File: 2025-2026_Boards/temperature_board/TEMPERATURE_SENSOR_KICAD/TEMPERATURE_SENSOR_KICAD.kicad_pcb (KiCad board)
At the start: 2 copper layers, 103 parts, among them J1 LCD Connector Pinout, J10 Conn_01x03_Pin, J11 Conn_01x03_Pin, J12 Conn_01x02_Pin, J13 Conn_01x02_Pin, J14 Conn_01x02_Pin, J15 Conn_01x02_Pin, J16 Conn_01x02_Pin, J17 Conn_01x02_Pin, J18 Conn_01x02_Pin, J19 Conn_01x02_Pin, J2 Conn_01x02_Pin, J20 Conn_01x02_Pin, J21 Conn_01x02_Pin, J22 Conn_01x02_Pin, J23 Conn_01x02_Pin, J24 Conn_01x02_Pin, J25 Conn_01x02_Pin, J3 Conn_01x02_Pin, J4 Conn_01x03_Pin, J5 Conn_01x03_Pin, J6 Conn_01x03_Pin, J7 Conn_01x03_Pin, J8 Conn_01x03_Pin, J9 Conn_01x03_Pin, U1 STM32G431CBT6, U2 TMP235A4DBZR, U3 AMS1117-3.3, U5 TPS62932DRLR, U6 TPS62932DRLR, U8 AMS1117

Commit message: Worked on PCB. Have to change some track widths.
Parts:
- added J4: Conn_01x02_Pin, Connector_JST:JST_EH_B2B-EH-A_1x02_P2.50mm_Vertical, F.Cu at (33.0, 90.0)
- added J4: Conn_01x02_Pin, Connector_JST:JST_EH_B2B-EH-A_1x02_P2.50mm_Vertical, F.Cu at (113.2, 85.2)
- added J5: Conn_01x02_Pin, Connector_JST:JST_EH_B2B-EH-A_1x02_P2.50mm_Vertical, F.Cu at (119.0, 85.2)
- added J5: Conn_01x02_Pin, Connector_JST:JST_EH_B2B-EH-A_1x02_P2.50mm_Vertical, F.Cu at (33.0, 95.8)
- added J6: Conn_01x02_Pin, Connector_JST:JST_EH_B2B-EH-A_1x02_P2.50mm_Vertical, F.Cu at (33.0, 101.7)
- added J6: Conn_01x02_Pin, Connector_JST:JST_EH_B2B-EH-A_1x02_P2.50mm_Vertical, F.Cu at (124.9, 85.2)
- added J7: Conn_01x02_Pin, Connector_JST:JST_EH_B2B-EH-A_1x02_P2.50mm_Vertical, F.Cu at (33.0, 107.5)
- added J7: Conn_01x02_Pin, Connector_JST:JST_EH_B2B-EH-A_1x02_P2.50mm_Vertical, F.Cu at (130.8, 85.2)
- added J8: Conn_01x02_Pin, Connector_JST:JST_EH_B2B-EH-A_1x02_P2.50mm_Vertical, F.Cu at (33.0, 113.3)
- moved Cboot2 607.3 mm to (58.5, 135.7)
- moved Cinx2 607.3 mm to (53.5, 136.5)
- moved L2 607.3 mm to (64.0, 143.5)
- moved Rfbt2 607.3 mm to (59.7, 134.0)
- moved U5 607.3 mm to (56.1, 135.2)
- moved Rfbb2 607.3 mm to (59.5, 132.5)
- moved Cout2 590.4 mm to (64.5, 134.5)
- moved Css2 590.1 mm to (56.8, 133.0)
- moved C1 518.3 mm to (175.0, 128.4)
- moved C2 518.3 mm to (175.0, 125.0)
- moved C3 518.3 mm to (175.5, 122.2)
- moved D1 518.3 mm to (174.0, 122.8)
- moved R1 518.3 mm to (173.3, 124.3), turned to -90 degrees
- moved U3 518.3 mm to (180.5, 124.0)
- moved J4 511.9 mm to (31.0, 50.0)
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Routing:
- net GND: track 6.56 -> 26.4 mm, vias 0 -> 18
- net +2.2V: track 2.56 -> 8.12 mm
- net Net-(U6-FB): track 0.00 -> 3.63 mm
- net Net-(U5-SS): track 0.00 -> 2.75 mm
- net 5V: track 13.0 -> 15.8 mm
- net 12V: track 13.4 -> 15.5 mm
- net Net-(U5-FB): track 2.06 -> 3.61 mm
- net +3.3V: track 11.2 -> 12.5 mm
- net /PWR_LED_K: track 0.00 -> 1.14 mm
- net Net-(D35-K): track 0.00 -> 1.04 mm

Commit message: Fan connectors broken+buggy. Fixed it. Accidentally deleted ground plane. Will have to add back. To get done by start of work session on Sunday: Hook up all fan connectors. Hook up temperature sensor to microcontroller. Hook up power distributor to microcontroller. At work session: Figure out LCD-diode wiring
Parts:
- removed J22, J23, J24, J25: Conn_01x02_Pin, Connector_JST:JST_EH_B2B-EH-A_1x02_P2.50mm_Vertical
- removed the J4 at (33.0, 90.0)
- removed the J4 at (113.2, 85.2)
- removed the J4 at (31.0, 50.0)
- removed the J5 at (31.0, 58.0)
- removed the J5 at (119.0, 85.2)
- removed the J5 at (33.0, 95.8)
- removed the J6 at (33.0, 101.7)
- removed the J6 at (31.0, 65.8)
- removed the J6 at (124.9, 85.2)
- removed the J7 at (33.0, 107.5)
- removed the J7 at (31.0, 73.8)
- removed the J7 at (130.8, 85.2)
- removed the J8 at (33.0, 113.3)
- removed the J8 at (31.0, 81.7)
- added J4: Conn_01x02_Pin, Connector:FanPinHeader_1x03_P2.54mm_Vertical, F.Cu at (21.5, 128.0)
- added J5: Conn_01x02_Pin, Connector:FanPinHeader_1x03_P2.54mm_Vertical, F.Cu at (21.5, 119.5)
- added J6: Conn_01x02_Pin, Connector:FanPinHeader_1x03_P2.54mm_Vertical, F.Cu at (21.5, 169.5)
- added J7: Conn_01x02_Pin, Connector:FanPinHeader_1x03_P2.54mm_Vertical, F.Cu at (21.5, 178.0)
- added J8: Conn_01x02_Pin, Connector:FanPinHeader_1x03_P2.54mm_Vertical, F.Cu at (21.5, 186.0)
- J10, J11, J9: value Conn_01x03_Pin -> Conn_01x02_Pin
- J12, J13, J14, J15, J16, J17, J18, J19, J2, J20, J21, J3: footprint Connector_JST:JST_EH_B2B-EH-A_1x02_P2.50mm_Vertical -> Connector:FanPinHeader_1x03_P2.54mm_Vertical
- moved J2 539.3 mm to (16.4, 193.5)
- moved J12 522.9 mm to (21.5, 161.0), turned to 180 degrees
- moved J14 517.8 mm to (21.5, 144.5), turned to 180 degrees
- moved J17 516.1 mm to (17.0, 88.5)
- moved J13 513.4 mm to (21.5, 103.0), turned to 180 degrees
- moved J16 455.4 mm to (79.8, 120.1)
- moved J15 439.4 mm to (95.4, 109.6)
- moved J3 438.7 mm to (94.9, 70.6)
- moved U2 276.1 mm to (164.9, 134.0)
- moved Cout1 152.9 mm to (74.7, 57.1), turned to 90 degrees
- moved Rfbb1 149.6 mm to (77.7, 58.6), turned to 0 degrees
- moved L3 148.4 mm to (86.0, 56.5), turned to 90 degrees
- moved Rfbt1 147.9 mm to (77.1, 60.1), turned to 0 degrees
- moved Css1 147.5 mm to (78.7, 59.9), turned to 90 degrees
- moved Cboot1 146.6 mm to (80.2, 60.1), turned to 0 degrees
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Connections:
- J10 pad 1: +12V -> 5V
- J10 pad 3: ECORE FAN PINS -> (no net)
- J11 pad 1: +12V -> 5V
- J11 pad 3: ECORE FAN PINS -> (no net)
- J12 pad 1: +12V -> 5V
- J13 pad 1: +12V -> 5V
- J14 pad 1: +12V -> 5V
- J15 pad 1: +12V -> 12V
- J16 pad 1: +12V -> 12V
- J17 pad 1: +12V -> 12V
- J18 pad 1: +5V -> 12V
- J19 pad 1: +5V -> 12V
- J2 pad 1: +12V -> 5V
- J20 pad 1: +5V -> 12V
- J21 pad 1: +5V -> 12V
- J3 pad 1: +12V -> 12V
- J9 pad 1: +12V -> 5V
- J9 pad 3: ECORE FAN PINS -> (no net)
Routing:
- net 5V: track 15.8 -> 99.5 mm
- net GND: track 26.4 -> 71.4 mm, vias 18 -> 30
- removed copper zone on B.Cu, net GND

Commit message: Kept wiring. To-do tomorrow: add back ground plane. Hook up ground vias. Wire LCD. Potentially reorganize the fan connectors. Wire fans together.
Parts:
- moved C13 453.5 mm to (42.5, 108.0)
- moved C8 449.7 mm to (49.0, 109.5), turned to 180 degrees
- moved C4 449.5 mm to (51.0, 108.5), turned to -90 degrees
- moved C9 448.6 mm to (49.0, 110.5), turned to 180 degrees
- moved C12 442.6 mm to (42.5, 107.0)
- moved C14 432.0 mm to (42.5, 103.0)
- moved R2 426.0 mm to (42.5, 104.0), turned to 180 degrees
- moved C11 422.1 mm to (42.3, 106.0)
- moved C10 411.2 mm to (49.0, 111.5)
- moved C5 405.1 mm to (52.0, 108.5), turned to -90 degrees
- moved FB1 402.6 mm to (47.0, 110.5), turned to -90 degrees
- moved C7 396.9 mm to (54.0, 108.5), turned to -90 degrees
- moved C6 393.3 mm to (53.0, 108.5), turned to -90 degrees
- moved C24 160.5 mm to (52.0, 156.4)
- moved C25 160.5 mm to (52.0, 154.0)
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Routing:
- net +3.3V: track 12.5 -> 48.2 mm
- net +3.3VA: track 0.00 -> 7.82 mm
- net Net-(U1-PA3): track 0.00 -> 2.94 mm
- net Net-(U2-VOUT): track 0.00 -> 1.98 mm
- net Net-(C10-Pad1): track 0.00 -> 1.63 mm
- net Net-(C8-Pad2): track 0.00 -> 1.00 mm

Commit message: Almost finished wiring. Just need to adjust widths and check configuration before finalizing design
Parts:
- removed D10, D11, D12, D13, D14, D15, D16, D17, D18, D19, D20, D21, D22, D23, D24, D25, D26, D27, D28, D29, D3, D30, D31, D32, D33, D34, D4, D5, D6, D7, D8, D9: 1N4148WT, Diode_SMD:D_SOD-523
- moved J1 393.8 mm to (59.9, 102.0), turned to 90 degrees
- moved J17 71.7 mm to (16.2, 20.5), turned to 90 degrees
- moved Cin1 64.3 mm to (22.8, 36.2), turned to -90 degrees
- moved Cin2 63.8 mm to (27.2, 31.2), turned to 0 degrees
- moved J19 62.8 mm to (84.8, 21.0), turned to 90 degrees
- moved J21 62.1 mm to (25.8, 20.5), turned to 90 degrees
- moved Cinx1 61.9 mm to (25.2, 35.8), turned to -90 degrees
- moved U6 60.0 mm to (27.9, 34.5), turned to 0 degrees
- moved Rfbt1 59.9 mm to (30.2, 32.1), turned to -90 degrees
- moved Cout1 59.5 mm to (33.2, 29.7), turned to 0 degrees
- moved Css1 58.0 mm to (30.5, 33.8), turned to 0 degrees
- moved Rfbb1 57.8 mm to (31.8, 32.8), turned to -90 degrees
- moved Cboot1 56.8 mm to (30.2, 35.2), turned to -90 degrees
- moved J20 54.8 mm to (74.8, 20.5), turned to 90 degrees
- moved J3 54.3 mm to (35.2, 20.5), turned to 90 degrees
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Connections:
- C1 pad 1: +5V -> 5V
- C24 pad 1: +5V -> 5V
- J1 pad 1: Net-(D15-K) -> Net-(J1-Pin_1)
- J1 pad 10: Net-(D16-K) -> Net-(J1-Pin_10)
- J1 pad 11: Net-(D11-K) -> Net-(J1-Pin_11)
- J1 pad 12: Net-(D10-A) -> Net-(J1-Pin_12)
- J1 pad 2: Net-(D14-K) -> Net-(J1-Pin_2)
- J1 pad 3: Net-(D10-K) -> Net-(J1-Pin_3)
- J1 pad 4: Net-(D13-K) -> Net-(J1-Pin_4)
- J1 pad 5: Net-(D17-K) -> Net-(J1-Pin_5)
- J1 pad 6: Net-(D27-A) -> Net-(J1-Pin_6)
- J1 pad 7: Net-(D12-K) -> Net-(J1-Pin_7)
- J1 pad 8: Net-(D19-A) -> Net-(J1-Pin_8)
- J1 pad 9: Net-(D11-A) -> Net-(J1-Pin_9)
- U1 pad 17: Net-(D12-K) -> unconnected-(U1-PB1-Pad17)
- U1 pad 25: unconnected-(U1-PB11-Pad25) -> Net-(J1-Pin_1)
- U1 pad 26: unconnected-(U1-PB12-Pad26) -> Net-(J1-Pin_2)
- U1 pad 27: unconnected-(U1-PB13-Pad27) -> Net-(J1-Pin_3)
- U1 pad 28: Net-(D27-A) -> Net-(J1-Pin_4)
- U1 pad 29: Net-(D19-A) -> Net-(J1-Pin_5)
- U1 pad 3: Net-(D11-K) -> unconnected-(U1-PC14-Pad3)
- U1 pad 30: unconnected-(U1-PA8-Pad30) -> Net-(J1-Pin_6)
- U1 pad 31: unconnected-(U1-PA9-Pad31) -> Net-(J1-Pin_7)
- U1 pad 32: unconnected-(U1-PA10-Pad32) -> Net-(J1-Pin_8)
- U1 pad 33: unconnected-(U1-PA11-Pad33) -> Net-(J1-Pin_9)
- U1 pad 34: unconnected-(U1-PA12-Pad34) -> Net-(J1-Pin_10)
- U1 pad 37: unconnected-(U1-PA13-Pad37) -> Net-(J1-Pin_11)
- U1 pad 38: unconnected-(U1-PA14-Pad38) -> Net-(J1-Pin_12)
- U1 pad 4: Net-(D16-K) -> unconnected-(U1-PC15-Pad4)
- U1 pad 40: Net-(D17-K) -> unconnected-(U1-PB3-Pad40)
- U1 pad 41: Net-(D13-K) -> unconnected-(U1-PB4-Pad41)
- U1 pad 42: Net-(D10-K) -> unconnected-(U1-PB5-Pad42)
- U1 pad 43: Net-(D14-K) -> unconnected-(U1-PB6-Pad43)
- U1 pad 44: Net-(D15-K) -> unconnected-(U1-PB7-Pad44)
- U1 pad 5: Net-(D11-A) -> unconnected-(U1-PF0-Pad5)
- U1 pad 7: Net-(D10-A) -> unconnected-(U1-PG10-Pad7)
- U3 pad 3: +5V -> 5V
- U8 pad 3: +5V -> 5V
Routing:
- net 5V: track 99.5 -> 193.6 mm
- net +3.3V: track 48.2 -> 57.6 mm
- net Net-(J1-Pin_12): track 0.00 -> 7.60 mm
- net GND: track 71.4 -> 78.1 mm, vias 30 -> 40
- net Net-(J1-Pin_11): track 0.00 -> 5.99 mm
- net +5V: track 5.47 -> 0.00 mm
- net Net-(J1-Pin_9): track 0.00 -> 3.79 mm
- net Net-(J1-Pin_8): track 0.00 -> 3.79 mm
- net Net-(J1-Pin_7): track 0.00 -> 3.79 mm
- net Net-(J1-Pin_6): track 0.00 -> 3.79 mm
- net Net-(J1-Pin_5): track 0.00 -> 3.79 mm
- net Net-(J1-Pin_4): track 0.00 -> 3.79 mm
- net Net-(J1-Pin_3): track 0.00 -> 3.79 mm
- net Net-(J1-Pin_2): track 0.00 -> 3.79 mm
- net Net-(J1-Pin_10): track 0.00 -> 3.79 mm
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
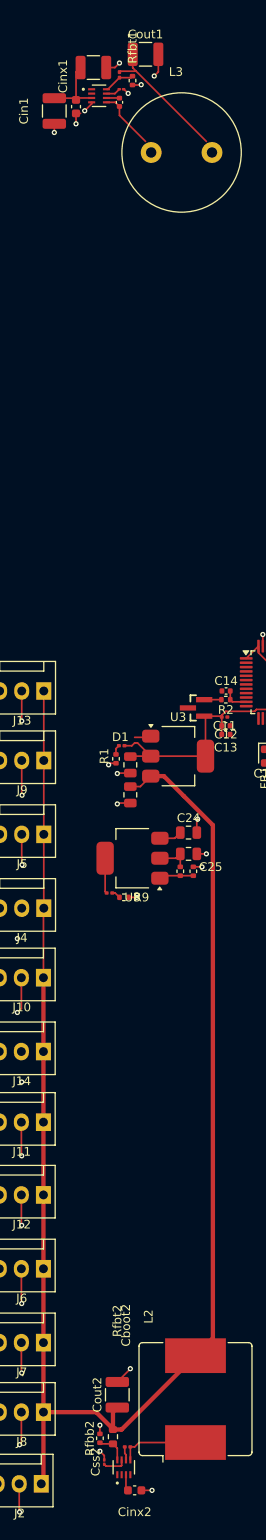
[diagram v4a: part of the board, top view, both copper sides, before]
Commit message: Adjusted widths for voltage safety.
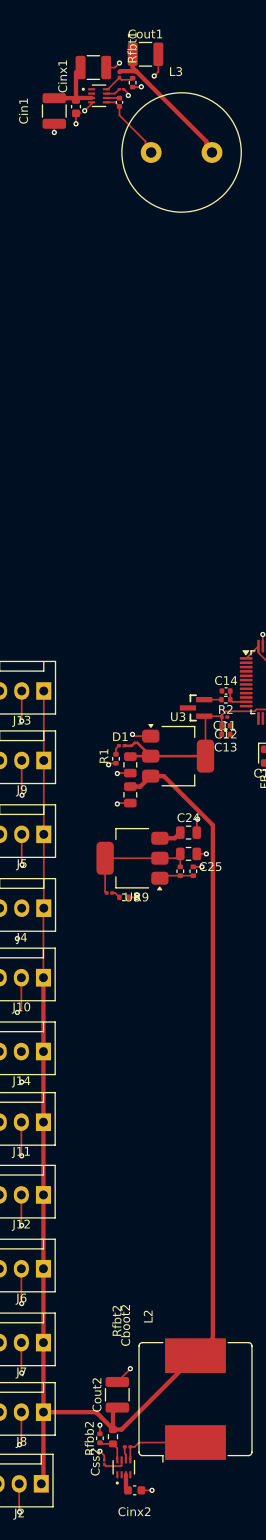
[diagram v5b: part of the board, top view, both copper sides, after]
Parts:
- moved Rfbb1 0.24 mm to (31.8, 33.0)
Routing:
- net +2.2V: track 8.12 -> 14.4 mm
- net Net-(U6-SW): track 6.96 -> 8.51 mm
- net 12V: track 15.5 -> 17.0 mm
- net GND: track 78.1 -> 78.6 mm, vias 40 -> 41
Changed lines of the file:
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@@
 		)
 		(property "Value" "47u"
-			(at 0 2.3 0)
+			(at 0.0175 2.54 0)
 			(layer "F.Fab")
 			(effects
@@
 	(footprint "Resistor_SMD:R_0402_1005Metric"
 		(layer "F.Cu")
-		(at 31.75 32.75 -90)
+		(at 31.7675 32.99 -90)
 		(descr "Resistor SMD 0402 (1005 Metric), square (rectangular) end terminal, IPC-7351 nominal, (Body size source: IPC-SM-782 page 72, https://www.pcb-3d.com/wordpress/wp-content/uploads/ipc-sm-782a_amendment_1_and_2.pdf), generated with kicad-footprint-generator")
 		(tags "resistor")
@@
 	)
 	(segment
+		(start 31.95 108.2)
+		(end 31.75 108)
+		(width 0.2)
+		(layer "F.Cu")
+		(net 1)
+	)
+	(segment
 		(start 31.5 112.45)
 		(end 30.05 112.45)
@@
 	)
 	(segment
-		(start 32 108.335)
-		(end 33.715 108.335)
-		(width 0.2)
-		(layer "F.Cu")
-		(net 1)
-	)
-	(segment
 		(start 27.0482 35.4268)
 		(end 26.25 36.225)
@@
 	)
 	(segment
+		(start 33.85 108.2)
+		(end 31.95 108.2)
+		(width 0.2)
+		(layer "F.Cu")
+		(net 1)
+	)
+	(segment
 		(start 51 108.98)
 		(end 51 110)
@@
 	)
 	(segment
-		(start 31.75 33.26)
-		(end 32.715 33.26)
+		(start 31.7675 33.5)
+		(end 32.7325 33.5)
 		(width 0.2)
 		(layer "F.Cu")
@@
 	)
 	(via
-		(at 32.75 33.225)
+		(at 32.7675 33.465)
+		(size 0.6)
+		(drill 0.3)
+		(layers "F.Cu" "B.Cu")
+		(net 1)
+	)
+	(via
+		(at 31.75 108)
 		(size 0.6)
 		(drill 0.3)
@@
 	)
 	(via
-		(at 31.25 34.225)
+		(at 31.2675 34.465)
 		(size 0.6)
 		(drill 0.3)
@@
 		(start 32.325 108.975)
 		(end 33.85 110.5)
-		(width 0.2)
+		(width 0.3)
 		(layer "F.Cu")
 		(net 2)
@@
 		(start 33.85 110.5)
 		(end 40.15 110.5)
-		(width 0.2)
+		(width 0.3)
 		(layer "F.Cu")
 		(net 2)
@@
 		(start 31.675 109.3)
 		(end 32 108.975)
-		(width 0.2)
+		(width 0.3)
 		(layer "F.Cu")
 		(net 2)
@@
 		(start 32 108.975)
 		(end 32.325 108.975)
-		(width 0.2)
+		(width 0.3)
 		(layer "F.Cu")
 		(net 2)
@@
 		(start 33.85 110.5)
 		(end 31.55 110.5)
-		(width 0.2)
+		(width 0.3)
 		(layer "F.Cu")
 		(net 2)
@@
 		(start 30.825 109.3)
 		(end 31.675 109.3)
-		(width 0.2)
+		(width 0.3)
 		(layer "F.Cu")
 		(net 2)
@@
 	)
 	(segment
+		(start 28.6 122.25)
+		(end 34.9 122.25)
+		(width 0.2)
+		(layer "F.Cu")
+		(net 7)
+	)
+	(segment
 		(start 36.75 122.25)
 		(end 34.9 122.25)
@@
 	)
 	(segment
+		(start 33.25 40.375711)
+		(end 33.8991 41.024811)
+		(width 0.2)
+		(layer "F.Cu")
+		(net 8)
+	)
+	(segment
+		(start 33.25 39.75)
+		(end 33.25 40.375711)
+		(width 0.2)
+		(layer "F.Cu")
+		(net 8)
+	)
+	(segment
 		(start 30.25 35.73)
 		(end 30.25 36.75)
@@
 		(start 22.75 34.775)
 		(end 25.05 34.775)
-		(width 0.2)
+		(width 0.5)
 		(layer "F.Cu")
 		(net 12)
@@
 		(start 25.25 34.975)
 		(end 25.25 31.775)
-		(width 0.2)
+		(width 0.5)
 		(layer "F.Cu")
 		(net 12)
@@
 		(start 25.475126 34.749874)
 		(end 27.0482 34.749874)
-		(width 0.2)
+		(width 0.5)
 		(layer "F.Cu")
 		(net 12)
@@
 		(start 30.999874 193.2018)
 		(end 30.999874 194.774874)
-		(width 0.2)
+		(width 0.5)
 		(layer "F.Cu")
 		(net 12)
@@
 		(start 32.169 31.669)
 		(end 30.356 31.669)
-		(width 0.2)
+		(width 0.5)
+		(layer "F.Cu")
+		(net 13)
+	)
+	(segment
+		(start 40.25 40.375711)
+		(end 40.8991 41.024811)
+		(width 0.5)
 		(layer "F.Cu")
 		(net 13)
@@
 		(start 40.25 39.75)
 		(end 32.169 31.669)
-		(width 0.2)
+		(width 0.5)
+		(layer "F.Cu")
+		(net 13)
+	)
+	(segment
+		(start 40.25 39.75)
+		(end 40.25 40.375711)
+		(width 0.5)
 		(layer "F.Cu")
 		(net 13)
@@
 		(start 30.356 31.669)
 		(end 30.25 31.775)
-		(width 0.2)
+		(width 0.5)
 		(layer "F.Cu")
 		(net 13)
@@
 		(start 31.775 31.275)
 		(end 32.169 31.669)
-		(width 0.2)
+		(width 0.5)
 		(layer "F.Cu")
 		(net 13)
@@
 		(start 31.775 29.725)
 		(end 31.775 31.275)
-		(width 0.2)
+		(width 0.5)
 		(layer "F.Cu")
 		(net 13)
@@
 		(start 31.5 114)
 		(end 32.65 114)
-		(width 0.2)
+		(width 0.5)
 		(layer "F.Cu")
 		(net 14)
@@
 		(start 36.6 119.95)
 		(end 34.9 119.95)
-		(width 0.2)
+		(width 0.5)
 		(layer "F.Cu")
 		(net 14)
@@
 		(start 32.65 114)
 		(end 33.85 112.8)
-		(width 0.2)
+		(width 0.5)
 		(layer "F.Cu")
 		(net 14)
@@
 		(start 37.25 119.3)
 		(end 36.6 119.95)
-		(width 0.2)
+		(width 0.5)
 		(layer "F.Cu")
 		(net 14)
@@
 	)
 	(segment
+		(start 30.5 32.655)
+		(end 30.49 32.655)
+		(width 0.2)
+		(layer "F.Cu")
+		(net 20)
+	)
+	(segment
 		(start 28.915378 33.749622)
 		(end 30.25 32.415)
@@
 	)
 	(segment
-		(start 31.575 32.415)
-		(end 31.75 32.24)
+		(start 31.5925 32.655)
+		(end 31.7675 32.48)
 		(width 0.2)
 		(layer "F.Cu")
@@
 	)
 	(segment
-		(start 30.25 32.415)
-		(end 31.575 32.415)
+		(start 30.5 32.655)
+		(end 31.5925 32.655)
+		(width 0.2)
+		(layer "F.Cu")
+		(net 20)
+	)
+	(segment
+		(start 30.49 32.655)
+		(end 30.25 32.415)
 		(width 0.2)
 		(layer "F.Cu")

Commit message: Finishing up
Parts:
- J2: footprint Connector:FanPinHeader_1x03_P2.54mm_Vertical -> Connector_JST:JST_EH_S2B-EH_1x02_P2.50mm_Horizontal
- moved J19 143.7 mm to (131.2, 157.0), turned to 0 degrees
- moved J20 138.7 mm to (131.8, 147.0), turned to 0 degrees
- moved J16 134.6 mm to (131.8, 137.5), turned to 0 degrees
- moved J17 134.0 mm to (131.8, 88.5), turned to 0 degrees
- moved J15 131.4 mm to (131.8, 127.0), turned to 0 degrees
- moved J21 131.3 mm to (131.8, 98.0), turned to 0 degrees
- moved J18 129.9 mm to (131.8, 117.0), turned to 0 degrees
- moved J3 129.9 mm to (131.8, 107.5), turned to 0 degrees
- moved Cout1 117.1 mm to (122.5, 105.5), turned to -90 degrees
- moved Cin2 116.0 mm to (121.0, 99.5), turned to -90 degrees
- moved Rfbt1 114.2 mm to (120.2, 102.5), turned to 180 degrees
- moved Rfbb1 112.7 mm to (119.3, 104.0), turned to 180 degrees
- moved Css1 111.8 mm to (118.5, 102.7), turned to -90 degrees
- moved U6 111.3 mm to (117.8, 100.1), turned to -90 degrees
- moved Cin1 110.2 mm to (116.0, 95.0), turned to 180 degrees
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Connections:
- U1 pad 13: unconnected-(U1-PA5-Pad13) -> +2.2V
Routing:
- net 5V: track 193.6 -> 122.2 mm
- net +2.2V: track 14.4 -> 34.3 mm

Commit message: minor updates
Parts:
- added C15: 100n, Capacitor_SMD:C_0402_1005Metric, F.Cu at (122.3, 145.2)
- added C16: 100n, Capacitor_SMD:C_0402_1005Metric, F.Cu at (122.3, 147.2)
- added J24: Conn_01x03_Socket, Connector_JST:JST_PH_S3B-PH-SM4-TB_1x03-1MP_P2.00mm_Horizontal, F.Cu at (114.8, 143.2)
- added J25: Conn_01x03_Socket, Connector_JST:JST_PH_S3B-PH-SM4-TB_1x03-1MP_P2.00mm_Horizontal, F.Cu at (114.8, 154.5)
- added U4: TCAN1057AEV-Q1, Package_SO:SOIC-8_3.9x4.9mm_P1.27mm, F.Cu at (125.1, 141.0)
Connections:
- U1 pad 14: unconnected-(U1-PA6-Pad14) -> Net-(J1-Pin_9)
- U1 pad 15: unconnected-(U1-PA7-Pad15) -> Net-(J1-Pin_10)
- U1 pad 33: Net-(J1-Pin_9) -> FDCAN_RX
- U1 pad 34: Net-(J1-Pin_10) -> FDCAN_TX
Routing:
- net Net-(J1-Pin_9): track 3.79 -> 0.00 mm
- net Net-(J1-Pin_10): track 3.79 -> 0.00 mm

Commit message: finishing the board. debuggign,ectc
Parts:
- added H1: MountingHole, MountingHole:MountingHole_4.3mm_M4, F.Cu at (139.5, 88.8)
- added H2: MountingHole, MountingHole:MountingHole_4.3mm_M4, F.Cu at (89.0, 93.2)
- added H3: MountingHole, MountingHole:MountingHole_4.3mm_M4, F.Cu at (87.5, 176.5)
- added H4: MountingHole, MountingHole:MountingHole_4.3mm_M4, F.Cu at (139.8, 177.0)
- added J22: Conn_01x02_Pin, Connector_AMASS:AMASS_XT30PW-M_1x02_P2.50mm_Horizontal, F.Cu at (110.5, 83.4)
- added J23: Conn_01x02_Pin, Connector_AMASS:AMASS_XT30PW-M_1x02_P2.50mm_Horizontal, F.Cu at (95.5, 83.5)
- added TP1: TestPoint, Connector_Pin:Pin_D1.3mm_L10.0mm_W3.5mm_Flat, F.Cu at (96.8, 125.8)
- added TP2: TestPoint, Connector_Pin:Pin_D1.3mm_L10.0mm_W3.5mm_Flat, F.Cu at (127.0, 110.2)
- added TP3: TestPoint, Connector_Pin:Pin_D1.3mm_L10.0mm_W3.5mm_Flat, F.Cu at (120.8, 114.0)
- added TP4: TestPoint, Connector_Pin:Pin_D1.3mm_L10.0mm_W3.5mm_Flat, F.Cu at (112.8, 140.8)
- J10, J11, J12, J13, J14, J15, J16, J17, J18, J19, J20, J21, J3, J4, J5, J6, J7, J8, J9: footprint Connector:FanPinHeader_1x03_P2.54mm_Vertical -> Connector_JST:JST_EH_S2B-EH_1x02_P2.50mm_Horizontal
- moved J25 81.4 mm to (134.4, 75.5), turned to 180 degrees
- moved J24 67.8 mm to (121.2, 75.8), turned to 180 degrees
- moved J17 14.9 mm to (137.0, 102.5), turned to -90 degrees
- moved C16 14.6 mm to (121.1, 132.6), turned to 90 degrees
- moved J21 14.6 mm to (137.2, 111.5), turned to -90 degrees
- moved J3 14.0 mm to (137.0, 120.5), turned to -90 degrees
- moved J18 13.9 mm to (137.2, 129.8), turned to -90 degrees
- moved J15 13.0 mm to (137.2, 138.8), turned to -90 degrees
- moved J16 11.9 mm to (137.0, 148.2), turned to -90 degrees
- moved C15 11.7 mm to (128.1, 135.1), turned to 90 degrees
- moved J20 11.5 mm to (137.0, 157.2), turned to -90 degrees
- moved J19 11.1 mm to (137.0, 166.5), turned to -90 degrees
- moved J2 7.64 mm to (80.3, 177.8), turned to 90 degrees
- moved J8 6.62 mm to (80.3, 168.2), turned to 90 degrees
- moved J7 5.56 mm to (80.3, 159.0), turned to 90 degrees
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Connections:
- C16 pad 1: 3.3 -> +3.3V
- U4 pad 5: 3.3 -> +3.3V
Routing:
- net 12V: track 17.0 -> 150.0 mm, vias 0 -> 1
- net 5V: track 122.2 -> 254.2 mm, vias 0 -> 2
- net 28V: track 10.3 -> 119.3 mm, vias 0 -> 1
- net CAN+: track 0.00 -> 84.4 mm
- net CAN-: track 0.00 -> 82.6 mm
- net +3.3V: track 57.6 -> 85.7 mm, vias 0 -> 2
- net Net-(J1-Pin_9): track 0.00 -> 23.4 mm, vias 0 -> 2
- net FDCAN_TX: track 0.00 -> 23.3 mm, vias 0 -> 2
- net Net-(J1-Pin_10): track 0.00 -> 19.4 mm, vias 0 -> 2
- net GND: track 78.6 -> 59.6 mm, vias 41 -> 38
- net FDCAN_RX: track 0.00 -> 17.7 mm, vias 0 -> 2
- net +2.2V: track 34.3 -> 40.4 mm
- net Net-(J1-Pin_8): track 3.79 -> 5.69 mm
- net Net-(J1-Pin_7): track 3.79 -> 5.69 mm
- net Net-(J1-Pin_6): track 3.79 -> 5.69 mm
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- added copper zone on B.Cu, net GND
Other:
- board outline added: 73 x 112.5 mm
